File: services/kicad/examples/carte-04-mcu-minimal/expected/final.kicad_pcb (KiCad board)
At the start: 2 copper layers, 38.8 x 30 mm, 15 parts, among them J1 IN_5V, J2 SWD, U1 STM32F103C8T6, U2 AMS1117-3.3

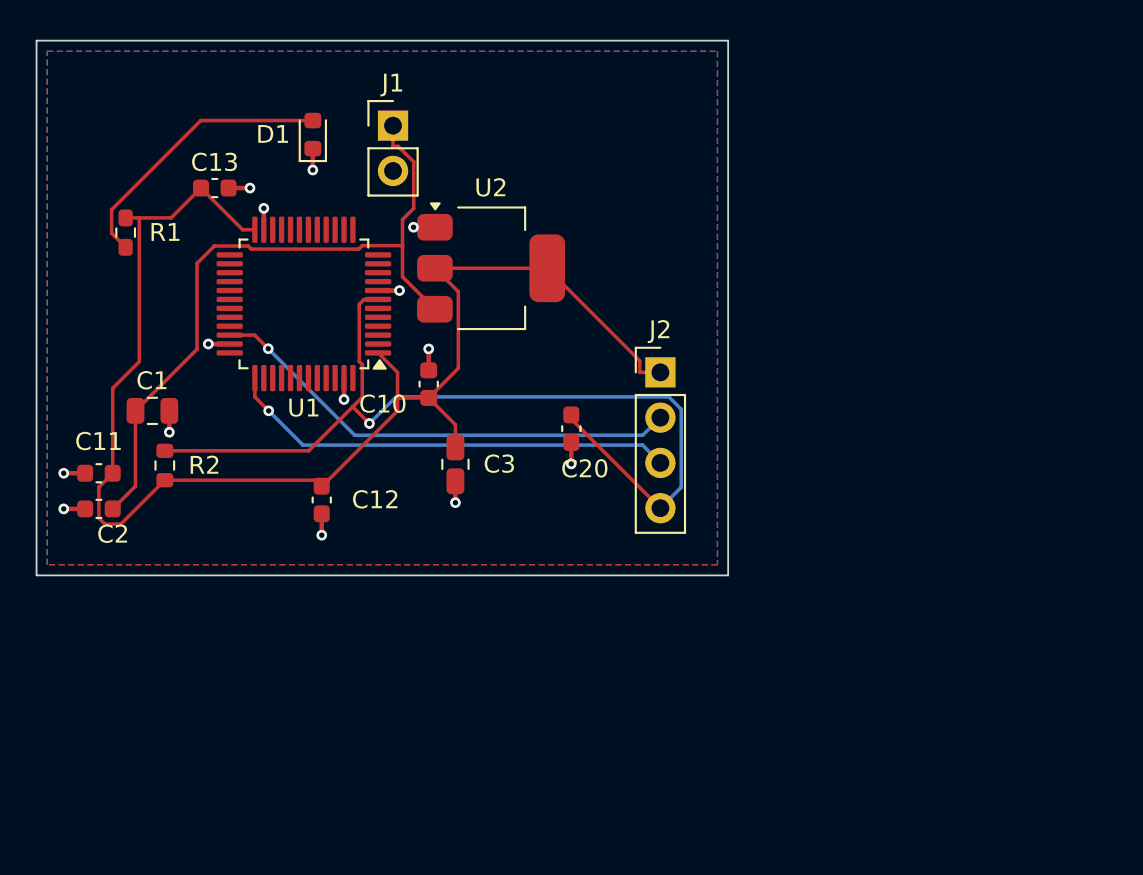
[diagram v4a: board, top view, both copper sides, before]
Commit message: fix(banc): le contour n etait JAMAIS resserre — dix cartes divisees par 2 a 4
Question de l utilisateur devant les rendus : « tu es satisfait de ce
placement ? ». Non, et la mesure lui donnait raison.

    carte-10 livree     140 x 105 mm = 14725 mm2
    son circuit          51 x  66 mm =  3366 mm2
    OCCUPATION                            23 %
    connecteurs                      56 a 75 mm du circuit
    fil de signal                      1230 mm  (VIN a lui seul 112 mm)

LA CAUSE : `run_pipeline.py` n envoyait pas `auto_size_board` a `/place/auto`.
Le resserrement du contour sur le placement existe depuis le 2026-09-13 et ne
s execute que si l appelant l autorise ; le defaut du modele est `False`.

C est le SEPTIEME levier de ce projet qui existe et que personne n appelle,
apres max_distance_mm, anchor_pin, WorkflowConfig.grid, constraints,
move_reference, bottom_up_placement et LocalRerouter.

⚠️ Et il etait INVISIBLE : la chaine de PRODUCTION passe bien le drapeau depuis
`handlePlacement`. Le banc mesurait donc un comportement que le produit n a
pas — l inverse exact de ce a quoi sert un banc.

MESURE APRES CORRECTION, meme circuit, meme graine :

    carte             demandee      REELLE        err  manq
    carte-01           25 x 20     20,1 x 14,6     0    0
    carte-02           55 x 40     34,9 x 25,4     0    0
    carte-03           50 x 35     26,1 x 20,1     0    0
    carte-04           60 x 45     36,6 x 27,2     0    0
    carte-05           70 x 50     43,6 x 32,6     0    0
    carte-06           80 x 60     48,5 x 36,4     0    0
    carte-07          110 x 80     53,2 x 38,8     0    0
    carte-08          125 x 95     56,4 x 44,1     0    0
    carte-09          130 x 100    57,3 x 45,2     0    0
    carte-10          140 x 105    61,0 x 45,8     0    0

Dix sur dix, 100 % route, aucune erreur, aucune connexion manquante. Sur
carte-10 : occupation 23 -> 56 %, fil de signal 1230 -> 652 mm, VIN 112 -> 45,5,
connecteurs 56-75 -> 23-35 mm.

ET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
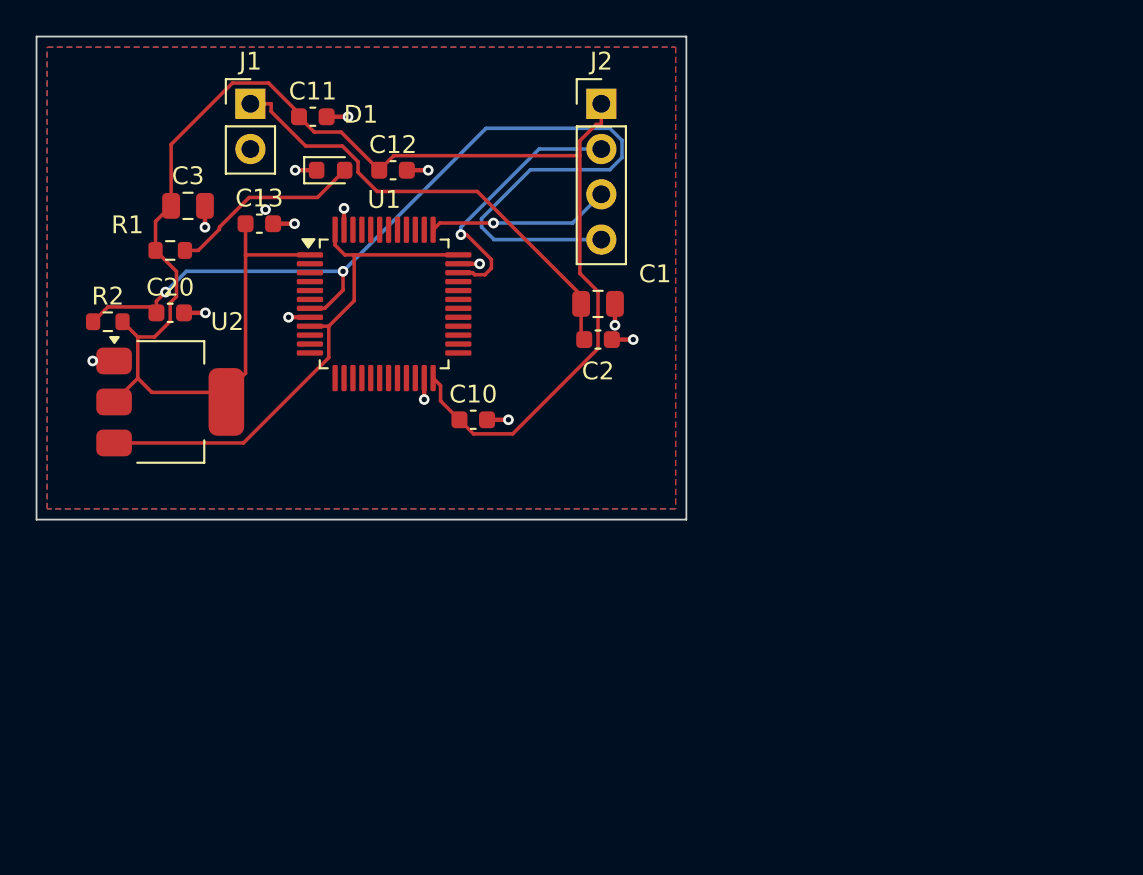
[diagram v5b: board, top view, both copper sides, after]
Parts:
- moved C2 29.6 mm to (150.0, 99.5), turned to 0 degrees
- moved C1 25.7 mm to (150.0, 97.5)
- moved C20 23.4 mm to (126.0, 98.0), turned to 0 degrees
- moved C11 23.3 mm to (134.0, 87.0), turned to 0 degrees
- moved C3 20.9 mm to (127.0, 92.0), turned to 0 degrees
- moved U2 19.5 mm to (126.0, 103.0)
- moved C12 18.9 mm to (138.5, 90.0), turned to 0 degrees
- moved J2 15.4 mm to (150.2, 86.3)
- moved R2 8.67 mm to (122.5, 98.5), turned to 0 degrees
- moved J1 8.09 mm to (130.5, 86.3)
- moved U1 4.50 mm to (138.0, 97.5), turned to 0 degrees
- moved C10 3.20 mm to (143.0, 104.0), turned to 0 degrees
- moved C13 3.20 mm to (131.0, 93.0)
- moved R1 2.69 mm to (126.0, 94.5), turned to 0 degrees
- moved D1 2.24 mm to (135.0, 90.0), turned to 0 degrees
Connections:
- U1 pad 36: Net-(U1-36) -> PWR_FLAG
- U1 pad 48: Net-(U1-48) -> PWR_FLAG
- U1 pad 9: Net-(U1-9) -> PWR_FLAG
- U2 pad 3: VIN -> PWR_FLAG
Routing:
- net PWR_FLAG: track 0.00 -> 29.4 mm
- net SWCLK: track 25.3 -> 10.3 mm
- net VIN: track 39.8 -> 26.2 mm
- net +3V3: track 79.3 -> 92.5 mm
- net SWDIO: track 26.9 -> 14.9 mm
- net LED_PWR: track 15.8 -> 10.9 mm
- net NRST: track 51.8 -> 56.2 mm, vias 1 -> 2
- net GND: vias 14 -> 15
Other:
- board size 38.8 x 30 mm -> 36.5 x 27.1 mm

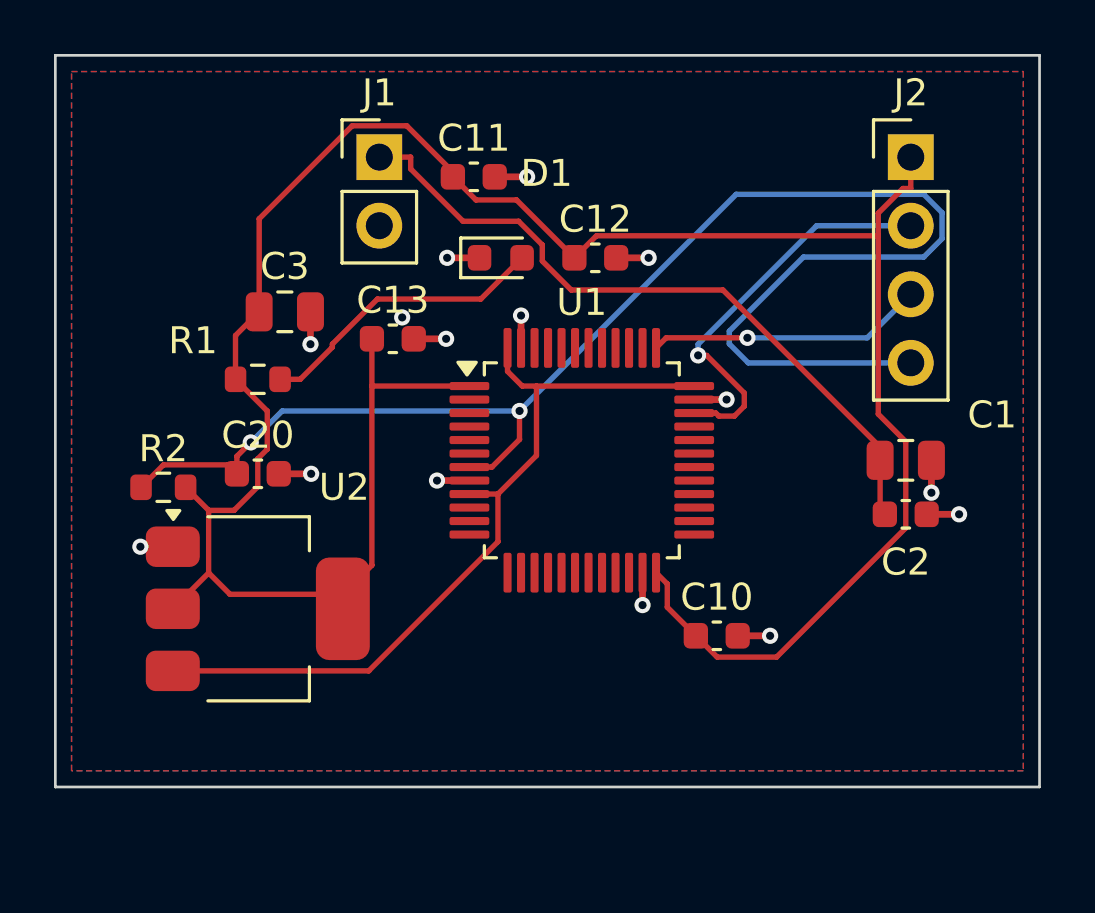
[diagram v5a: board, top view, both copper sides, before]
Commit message: feat(placement): les peripheriques se REPARTISSENT, ils ne s empilent plus
Question de l utilisateur devant le rendu : « c est quoi ce type de placement ? ».
Les composants s entassaient d un seul cote du boitier, etiquettes de
serigraphie l une sur l autre, trois quarts de la couronne vides.

TROIS CAUSES, toutes dans `_poser_les_peripheriques`, toutes la meme faute —
un angle unique pour tout un groupe :

  - les DIRECTS qui visent la meme broche (tous les decouplages d un rail,
    toutes les resistances d un meme signal) recevaient le MEME `angle_vers`
    et le meme rayon de depart ;
  - les SUIVEURS d un meme parent recevaient tous atan2(parent - centre) ;
  - les ISOLES partaient tous de l angle 0.0, c est-a-dire du meme point.

`le_long_du_rayon` ne s ecartait qu une fois la place prise : d ou la file.

REMEDE : `_ecart_en_eventail`. Le PREMIER de chaque groupe garde EXACTEMENT la
direction calculee — c est la topologie, on ne la perd pas pour faire joli — et
les suivants s ecartent symetriquement de 3 x `_PAS_ANGLE_DEG`.
Rien de deja pose ne bouge : seul l ANGLE DE DEPART de la recherche change, et
`le_long_du_rayon` reste seul juge de ce qui est libre.

BANC DES DIX CARTES, contour resserre ET peripheriques repartis :

    carte             demandee    livree         err  manq
    carte-01           25 x 20    20,1 x 13,6     0    0
    carte-02           55 x 40    34,9 x 25,2     0    0
    carte-03           50 x 35    27,6 x 19,9     0    0
    carte-04           60 x 45    36,6 x 29,8     0    0
    carte-05           70 x 50    40,0 x 32,6     0    0
    carte-06           80 x 60    46,5 x 36,4     0    0
    carte-07          110 x 80    47,7 x 38,8     0    0
    carte-08          125 x 95    57,4 x 44,1     0    0
    carte-09          130 x 100   57,8 x 45,2     0    0
    carte-10          140 x 105   59,0 x 45,8     0    0

Dix sur dix, 100 % route. carte-07 gagne 5,5 mm de largeur sur le passage
precedent, carte-06 deux, carte-10 deux. Sur ca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
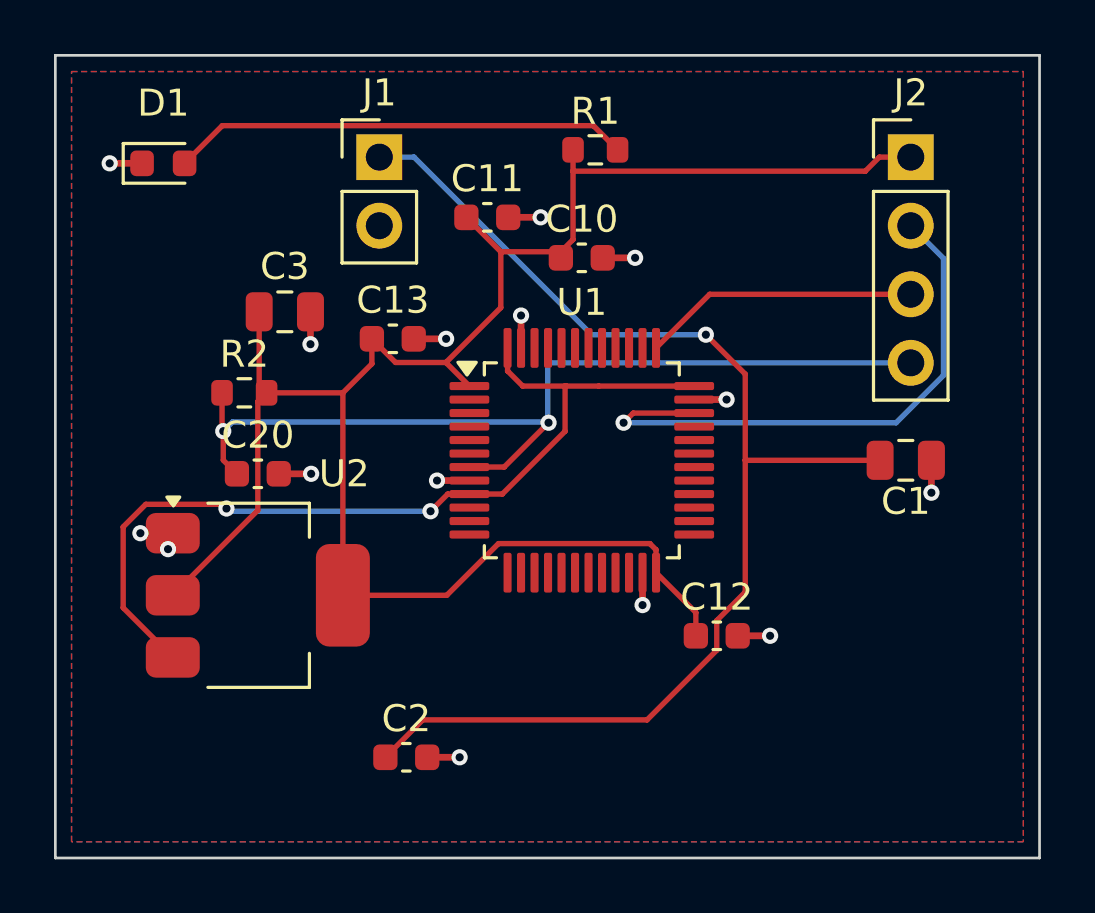
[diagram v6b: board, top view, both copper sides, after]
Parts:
- moved C2 20.6 mm to (131.5, 108.5)
- moved R1 15.1 mm to (138.5, 86.0)
- moved C10 14.9 mm to (138.0, 90.0)
- moved C12 14.7 mm to (143.0, 104.0)
- moved D1 13.0 mm to (122.5, 86.5)
- moved R2 4.61 mm to (125.5, 95.0)
- moved C11 1.58 mm to (134.5, 88.5)
- moved U2 0.50 mm to (126.0, 102.5)
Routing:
- net NRST: track 56.2 -> 34.7 mm
- net +3V3: track 92.5 -> 71.3 mm
- net VIN: track 26.2 -> 46.5 mm, vias 0 -> 1
- net SWDIO: track 14.9 -> 21.4 mm
- net LED_PWR: track 10.9 -> 17.0 mm
- net PWR_FLAG: track 29.4 -> 33.3 mm, vias 0 -> 2
- net SWCLK: vias 1 -> 0
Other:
- board size 36.5 x 27.1 mm -> 36.5 x 29.7 mm

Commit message: docs(banc): les dix boards du banc du 2026-09-23, service corrige
Artefacts du banc dont le tableau est deja commite : les dix cartes a
100 % route, 0 erreur, 0 connexion manquante, chacune a la taille de son
circuit.

Co-Authored-By: Claude Opus 5 <noreply@anthropic.com>
Claude-Session: https://claude.ai/code/session_01TnMqm4La2CxQHHB5K8aSSV
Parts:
- moved C10 11.3 mm to (127.0, 92.5)
- moved C3 8.73 mm to (135.0, 88.5)
- moved C11 5.15 mm to (139.0, 91.0)
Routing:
- net +3V3: track 71.3 -> 82.5 mm
- net PWR_FLAG: track 33.3 -> 28.1 mm, vias 2 -> 3
- net NRST: track 34.7 -> 39.4 mm
- net VIN: track 46.5 -> 42.5 mm
- net GND: vias 15 -> 14

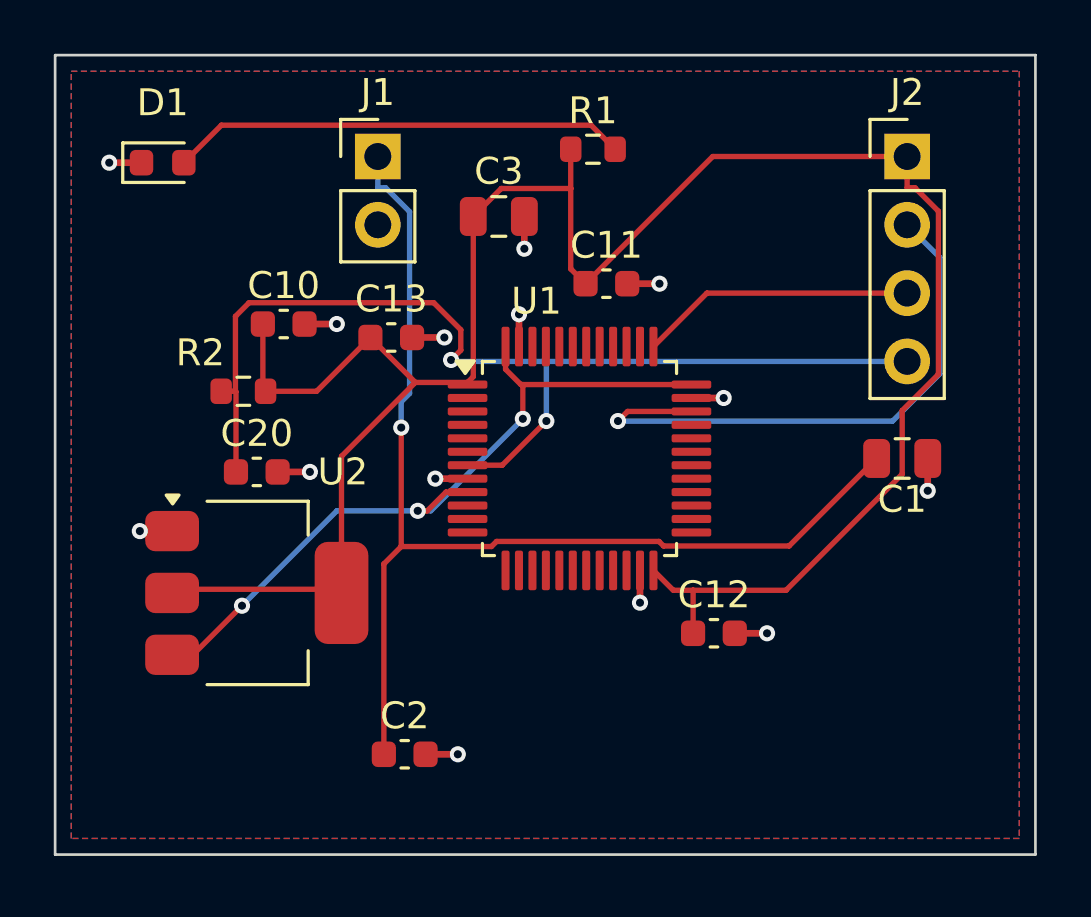
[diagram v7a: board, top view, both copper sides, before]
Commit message: fix(banc): le banc route comme la production — plafond 8, budget du client
D-2026-09-24-f. run_pipeline.py prenait 2 couches et 1800 s par défaut, et
carte-07 écrivait 2 en dur : dix cartes sur quinze ne pouvaient jamais
escalader, et la règle « toute connexion manquante fait monter » était
inerte dans le banc. Mesuré sur carte-07 : 97 %, seule la masse manquante,
« le palier suivant sera tenté »… puis retour à 2 couches.

Plafond par défaut 8 (client Pro Max), budget min(600 + 300 x plafond, 3600)
comme routingSearchBudgetS côté client. En production, rien ne change : le
plafond reste celui du plan.

Livraisons du jour, toutes vérifiées par kicad-cli et contre le schéma
(0 erreur bloquante, 0 connexion manquante, 0 court-circuit) :
carte-04, 05, 06, 08 (campagne de l'après-midi) et carte-09, 10 (4 couches).
Les boards versionnés de ces cartes court-circuitaient des nets du schéma.

Correction de ma propre erreur dans la doc : carte-07 n'avait jamais
escaladé ; les lignes « palier 4 et 6 » du journal étaient celles de
carte-08, démarrée la même minute.

Co-Authored-By: Claude Opus 5.5 <noreply@anthropic.com>
Claude-Session: https://claude.ai/code/session_01TnMqm4La2CxQHHB5K8aSSV
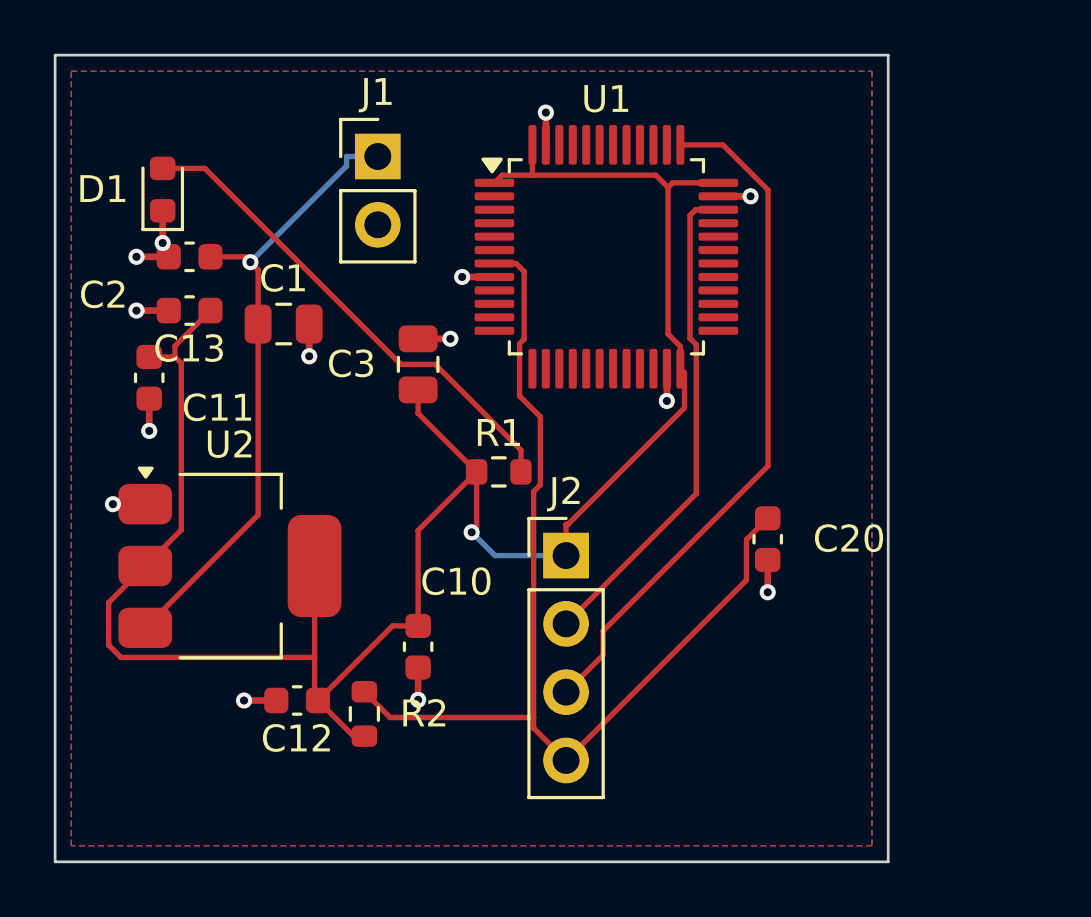
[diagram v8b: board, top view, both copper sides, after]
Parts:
- moved C1 23.5 mm to (127.0, 92.5)
- moved C2 20.2 mm to (123.5, 90.0), turned to 180 degrees
- moved J2 19.5 mm to (137.5, 101.1)
- moved C20 19.2 mm to (145.0, 100.5), turned to -90 degrees
- moved C11 17.4 mm to (122.0, 94.5), turned to -90 degrees
- moved C12 15.7 mm to (127.5, 106.5), turned to 180 degrees
- moved C10 13.0 mm to (132.0, 104.5), turned to -90 degrees
- moved R2 12.8 mm to (130.0, 107.0), turned to -90 degrees
- moved R1 12.5 mm to (135.0, 98.0)
- moved C13 7.57 mm to (123.5, 92.0), turned to 180 degrees
- moved U1 7.57 mm to (139.0, 90.0)
- moved C3 6.26 mm to (132.0, 94.0), turned to 90 degrees
- moved U2 1.41 mm to (125.0, 101.5)
- moved D1 1.00 mm to (122.5, 87.5), turned to 90 degrees
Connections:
- U1 pad 36: PWR_FLAG -> +3V3
- U1 pad 48: PWR_FLAG -> +3V3
- U1 pad 9: PWR_FLAG -> Net-(U1-9)
- U2 pad 3: PWR_FLAG -> VIN
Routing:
- net PWR_FLAG: track 28.1 -> 0.00 mm, vias 3 -> 0
- net VIN: track 42.5 -> 23.6 mm
- net SWCLK: track 10.3 -> 25.7 mm
- net +3V3: track 82.5 -> 77.6 mm, vias 0 -> 1
- net SWDIO: track 21.6 -> 18.4 mm, vias 1 -> 0
- net LED_PWR: track 17.0 -> 18.5 mm
- net NRST: track 39.4 -> 39.2 mm, vias 2 -> 0
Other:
- board size 36.5 x 29.7 mm -> 31 x 30 mm
